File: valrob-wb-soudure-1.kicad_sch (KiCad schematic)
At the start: 2 parts, among them J1 Conn_01x03

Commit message: schem: add tvs part #
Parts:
- D1: Basic (none) -> Z; JLCPCB Part # (none) -> C28485754; Manufacturer (none) -> Littelfuse; Manufacturer Part Number (none) -> P4KE7.5CA
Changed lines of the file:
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@@
+			)
+		)
+		(property "Basic" ""
+			(at 44.45 91.44 0)
+			(hide yes)
+			(show_name no)
+			(do_not_autoplace no)
+			(effects
+				(font
+					(size 1.27 1.27)
+				)
+			)
+		)
+		(property "JLCPCB Part #" ""
+			(at 44.45 91.44 0)
+			(hide yes)
+			(show_name no)
+			(do_not_autoplace no)
+			(effects
+				(font
+					(size 1.27 1.27)
+				)
+			)
+		)
+		(property "Manufacturer" ""
+			(at 44.45 91.44 0)
+			(hide yes)
+			(show_name no)
+			(do_not_autoplace no)
+			(effects
+				(font
+					(size 1.27 1.27)
+				)
+			)
+		)
+		(property "Manufacturer Part Number" ""
+			(at 44.45 91.44 0)
+			(hide yes)
+			(show_name no)
+			(do_not_autoplace no)
+			(effects
+				(font
+					(size 1.27 1.27)
+				)
 			)
 		)
@@
 			(hide yes)
 			(show_name no)
+			(do_not_autoplace no)
+			(effects
+				(font
+					(size 1.27 1.27)
+				)
+			)
+		)
+		(property "Basic" "Z"
+			(at 55.88 99.06 90)
+			(hide yes)
+			(show_name no)
+			(do_not_autoplace no)
+			(effects
+				(font
+					(size 1.27 1.27)
+				)
+			)
+		)
+		(property "JLCPCB Part #" "C28485754"
+			(at 55.88 99.06 90)
+			(hide yes)
+			(show_name no)
+			(do_not_autoplace no)
+			(effects
+				(font
+					(size 1.27 1.27)
+				)
+			)
+		)
+		(property "Manufacturer" "Littelfuse"
+			(at 55.88 99.06 90)
+			(hide yes)
+			(show_name no)
+			(do_not_autoplace no)
+			(effects
+				(font
+					(size 1.27 1.27)
+				)
+			)
+		)
+		(property "Manufacturer Part Number" "P4KE7.5CA"
+			(at 55.88 99.06 90)
+			(hide yes)
+			(show_name no)

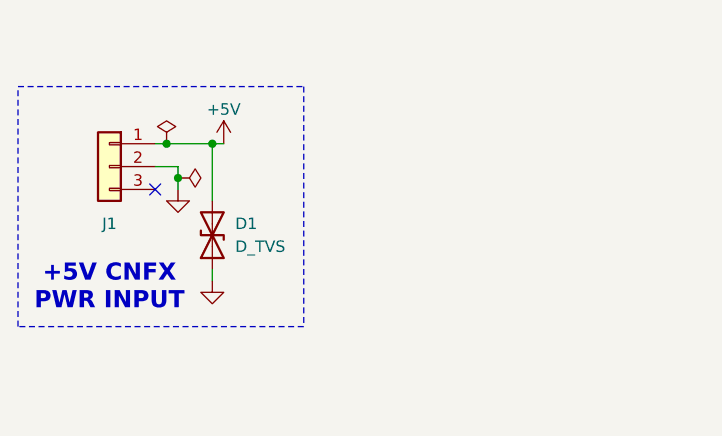
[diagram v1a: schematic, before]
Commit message: schem: add alt leds
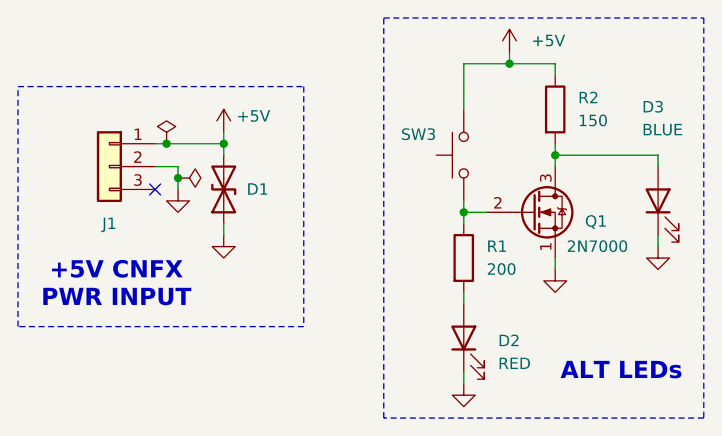
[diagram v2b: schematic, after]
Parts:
- added D2: RED, LED_THT:LED_D3.0mm, symbol Device:LED
- added D3: BLUE, LED_THT:LED_D3.0mm, symbol Device:LED
- added Q1: 2N7000, Package_TO_SOT_THT:TO-92_Inline, symbol Transistor_FET:2N7000
- added R1: 200, Resistor_THT:R_Axial_DIN0207_L6.3mm_D2.5mm_P10.16mm_Horizontal, symbol Device:R
- added R2: 150, Resistor_THT:R_Axial_DIN0207_L6.3mm_D2.5mm_P10.16mm_Horizontal, symbol Device:R
- added SW3: SW_Push, Button_Switch_THT:SW_SPST_Omron_B3F-40xx, symbol Switch:SW_Push
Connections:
- net +5V: now also R2.1, SW3.1
- net GND: now also D2.1 (K), D3.1 (K), Q1.1 (S)
- new net: Q1.2 (G), R1.1, SW3.2
- new net: D3.2 (A), Q1.3 (D), R2.2
- new net: D2.2 (A), R1.2
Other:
- note added: "ALT LEDs"
- moved on the sheet: D1

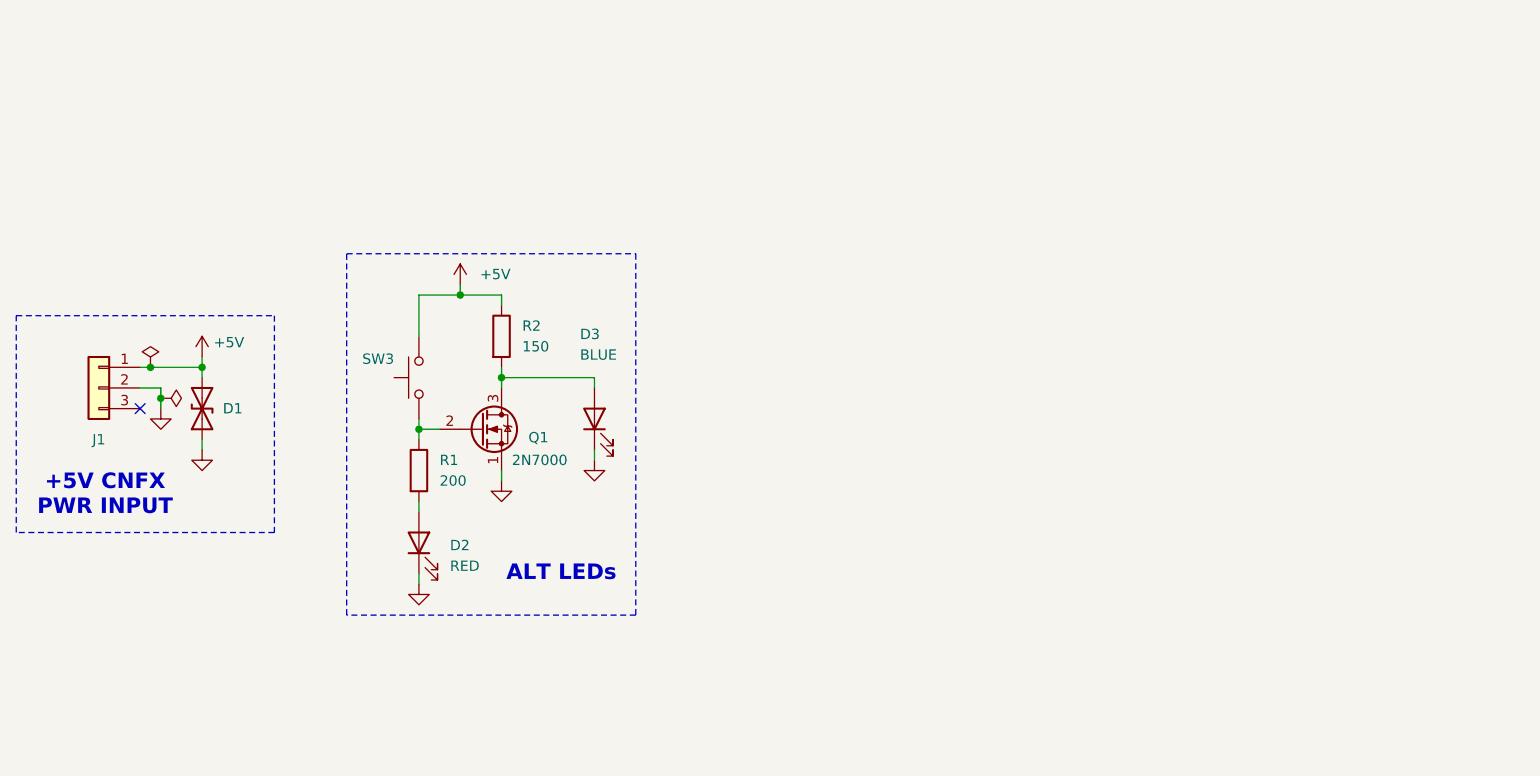
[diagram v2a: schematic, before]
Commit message: schem: add smt leds
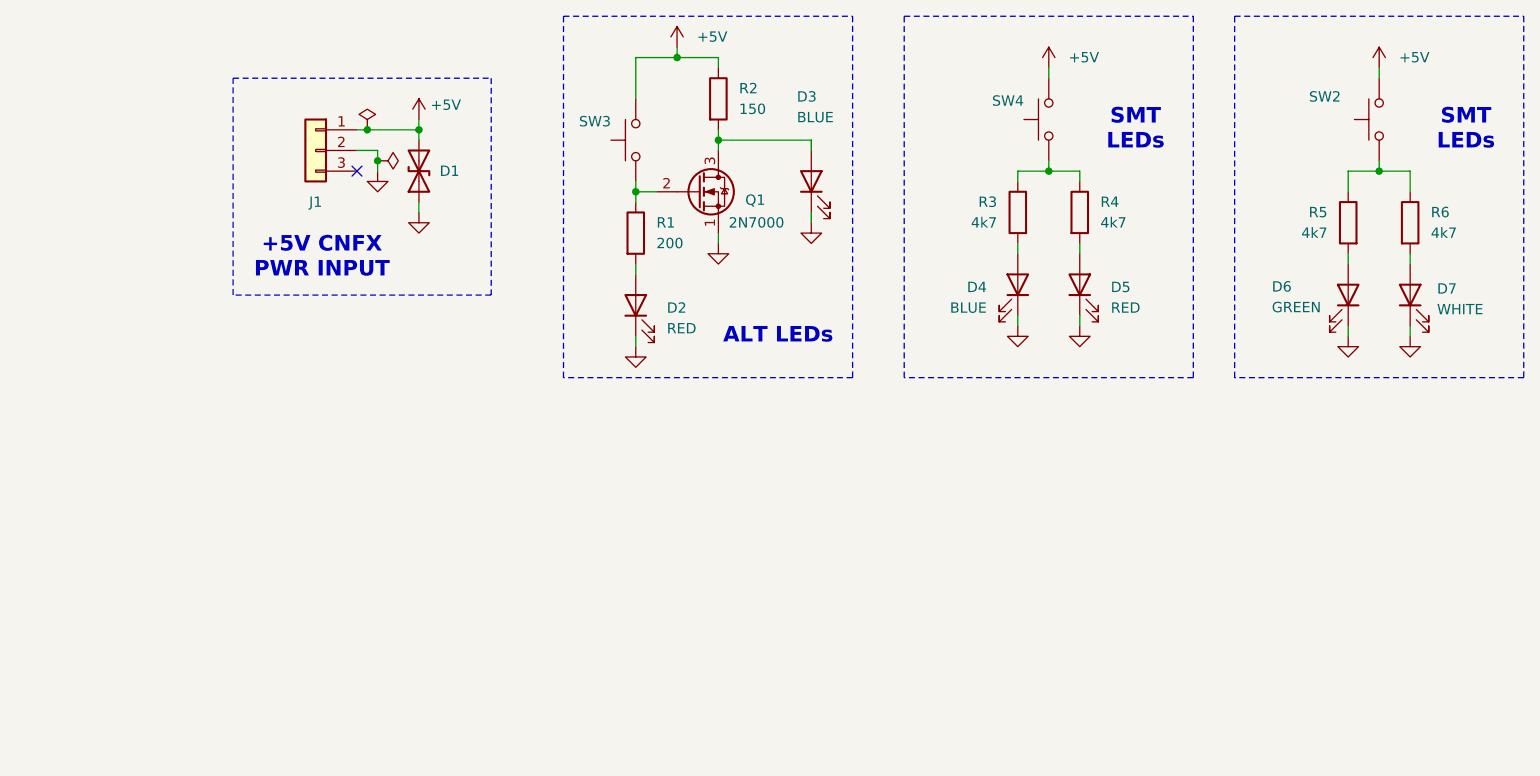
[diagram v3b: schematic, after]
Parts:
- added D4: BLUE, LED_SMD:LED_1206_3216Metric_Pad1.42x1.75mm_HandSolder, symbol Device:LED
- added D5: RED, LED_SMD:LED_1206_3216Metric_Pad1.42x1.75mm_HandSolder, symbol Device:LED
- added D6: GREEN, LED_SMD:LED_0805_2012Metric, symbol Device:LED
- added D7: WHITE, LED_SMD:LED_0603_1608Metric, symbol Device:LED
- added R3, R4, R5, R6: 4k7, Resistor_SMD:R_1206_3216Metric_Pad1.30x1.75mm_HandSolder, symbol Device:R
- added SW2: SW_Push, Button_Switch_SMD:SW_SPST_TS-1088-xR020, symbol Switch:SW_Push
- added SW4: SW_Push, Button_Switch_THT:SW_SPST_Omron_B3F-40xx, symbol Switch:SW_Push
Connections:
- net +5V: now also SW2.1, SW4.1
- net GND: now also D4.1 (K), D5.1 (K), D6.1 (K), D7.1 (K)
- new net: R3.1, R4.1, SW4.2
- new net: D5.2 (A), R4.2
- new net: R5.1, R6.1, SW2.2
- new net: D6.2 (A), R5.2
- new net: D7.2 (A), R6.2
- new net: D4.2 (A), R3.2
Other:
- note added: "SMT LEDs"
- moved on the sheet: D1, D2, D3, J1, Q1, R1, R2, SW3

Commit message: schem: add IOs
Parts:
- added D8: BLUE, LED_THT:LED_D3.0mm, symbol Device:LED
- added D9: RED, LED_THT:LED_D3.0mm, symbol Device:LED
- added J2: Conn_01x06, Package_TO_SOT_THT:TO-92_Inline, symbol Connector_Generic:Conn_01x06
- added R7: 150, Resistor_THT:R_Axial_DIN0207_L6.3mm_D2.5mm_P10.16mm_Horizontal, symbol Device:R
- added R8: 200, Resistor_THT:R_Axial_DIN0207_L6.3mm_D2.5mm_P10.16mm_Horizontal, symbol Device:R
- added RV1: 10k, Package_SO:TSSOP-20_4.4x6.5mm_P0.65mm, symbol Device:R_Potentiometer_Small
- added SW5: SW_Push, Button_Switch_THT:SW_SPST_Omron_B3F-40xx, symbol Switch:SW_Push
- added TP1: TestPoint, Package_TO_SOT_SMD:SOT-23-5, symbol Connector:TestPoint
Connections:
- net +5V: now also J2.6 (Pin_6), RV1.3
- net GND: now also D8.1 (K), D9.1 (K), J2.1 (Pin_1), RV1.1, SW5.2
- new net: D9.2 (A), R8.2
- new net: D8.2 (A), R7.2
- new net: J2.3 (Pin_3), RV1.2
- new net: J2.2 (Pin_2), SW5.1
- new net BLUE: J2.4 (Pin_4), R7.1
- new net RED: J2.5 (Pin_5), R8.1
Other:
- note added: "IOs"

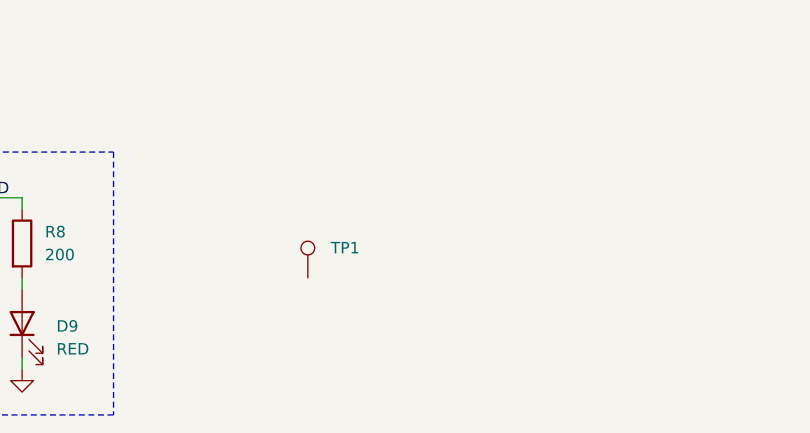
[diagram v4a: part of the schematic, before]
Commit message: schem: add test conns
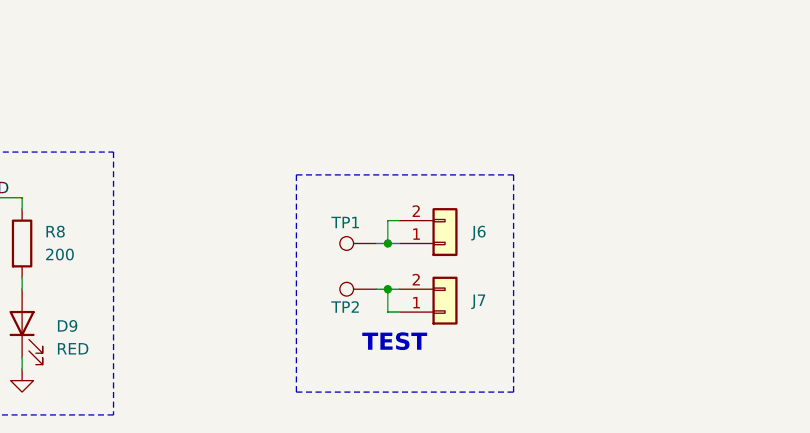
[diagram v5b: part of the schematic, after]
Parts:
- added J6, J7: Conn_01x02, TerminalBlock_Phoenix:TerminalBlock_Phoenix_MKDS-1,5-2-5.08_1x02_P5.08mm_Horizontal, symbol Connector_Generic:Conn_01x02
- added TP2: TestPoint, TestPoint:TestPoint_Loop_D3.50mm_Drill1.4mm_Beaded, symbol Connector:TestPoint
- TP1: footprint Package_TO_SOT_SMD:SOT-23-5 -> TestPoint:TestPoint_Loop_D3.50mm_Drill1.4mm_Beaded; Basic (none) -> Z; JLCPCB Part # (none) -> C5199814; Manufacturer (none) -> ronghe; Manufacturer Part Number (none) -> RH-5011
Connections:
- net at TP1.1: now also J6.1 (Pin_1), J6.2 (Pin_2)
- new net: J7.1 (Pin_1), J7.2 (Pin_2), TP2.1
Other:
- note added: "TEST"
- moved on the sheet: TP1

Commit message: schem: add jst connectors to test
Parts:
- added J4, J5: Conn_01x02, Connector_JST:JST_XH_B2B-XH-A_1x02_P2.50mm_Vertical, symbol Connector_Generic:Conn_01x02
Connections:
- net at J6.1 (Pin_1), J6.2 (Pin_2), TP1.1: now also J4.1 (Pin_1), J4.2 (Pin_2)
- net at J7.1 (Pin_1), J7.2 (Pin_2), TP2.1: now also J5.1 (Pin_1), J5.2 (Pin_2)
